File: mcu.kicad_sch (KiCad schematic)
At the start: 24 parts, among them J2 SWD_HIL, SW1 BTN1, SW2 BTN2, U8 STM32G431MBT6

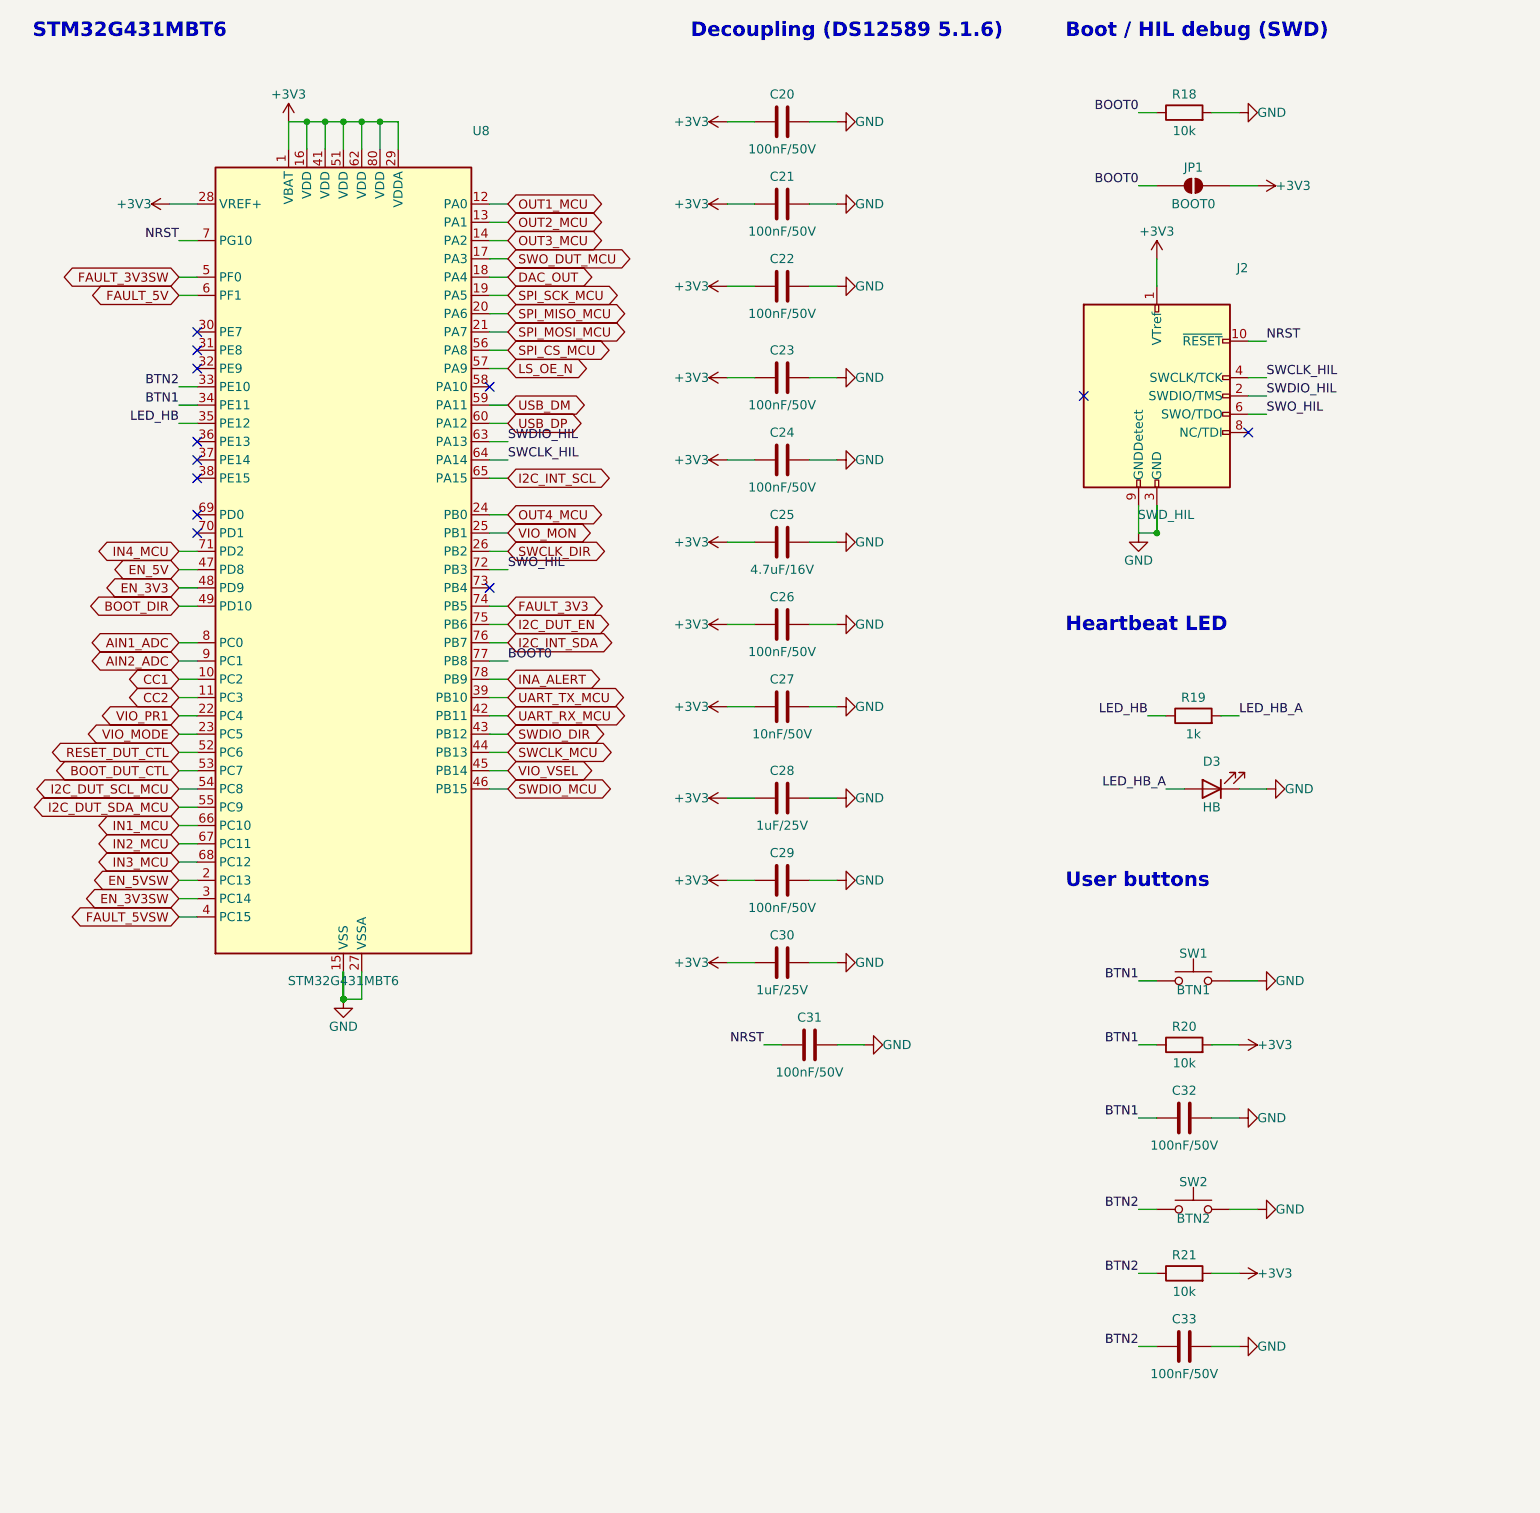
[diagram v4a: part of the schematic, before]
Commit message: feat: dual-range current sensing and fixed-rail readback in the schematic (TASK-011)
New sheets range_5v_sw, range_3v3_sw and readback appended at the end of the
hierarchy (existing references unchanged). Shunts now end on *_MID, INA226
Vin- on *_MID, MCU pins remapped per NOTES.md. ERC 0 errors, netlist and BOM
0 mismatches.

Co-Authored-By: Claude Opus 5.5 <noreply@anthropic.com>
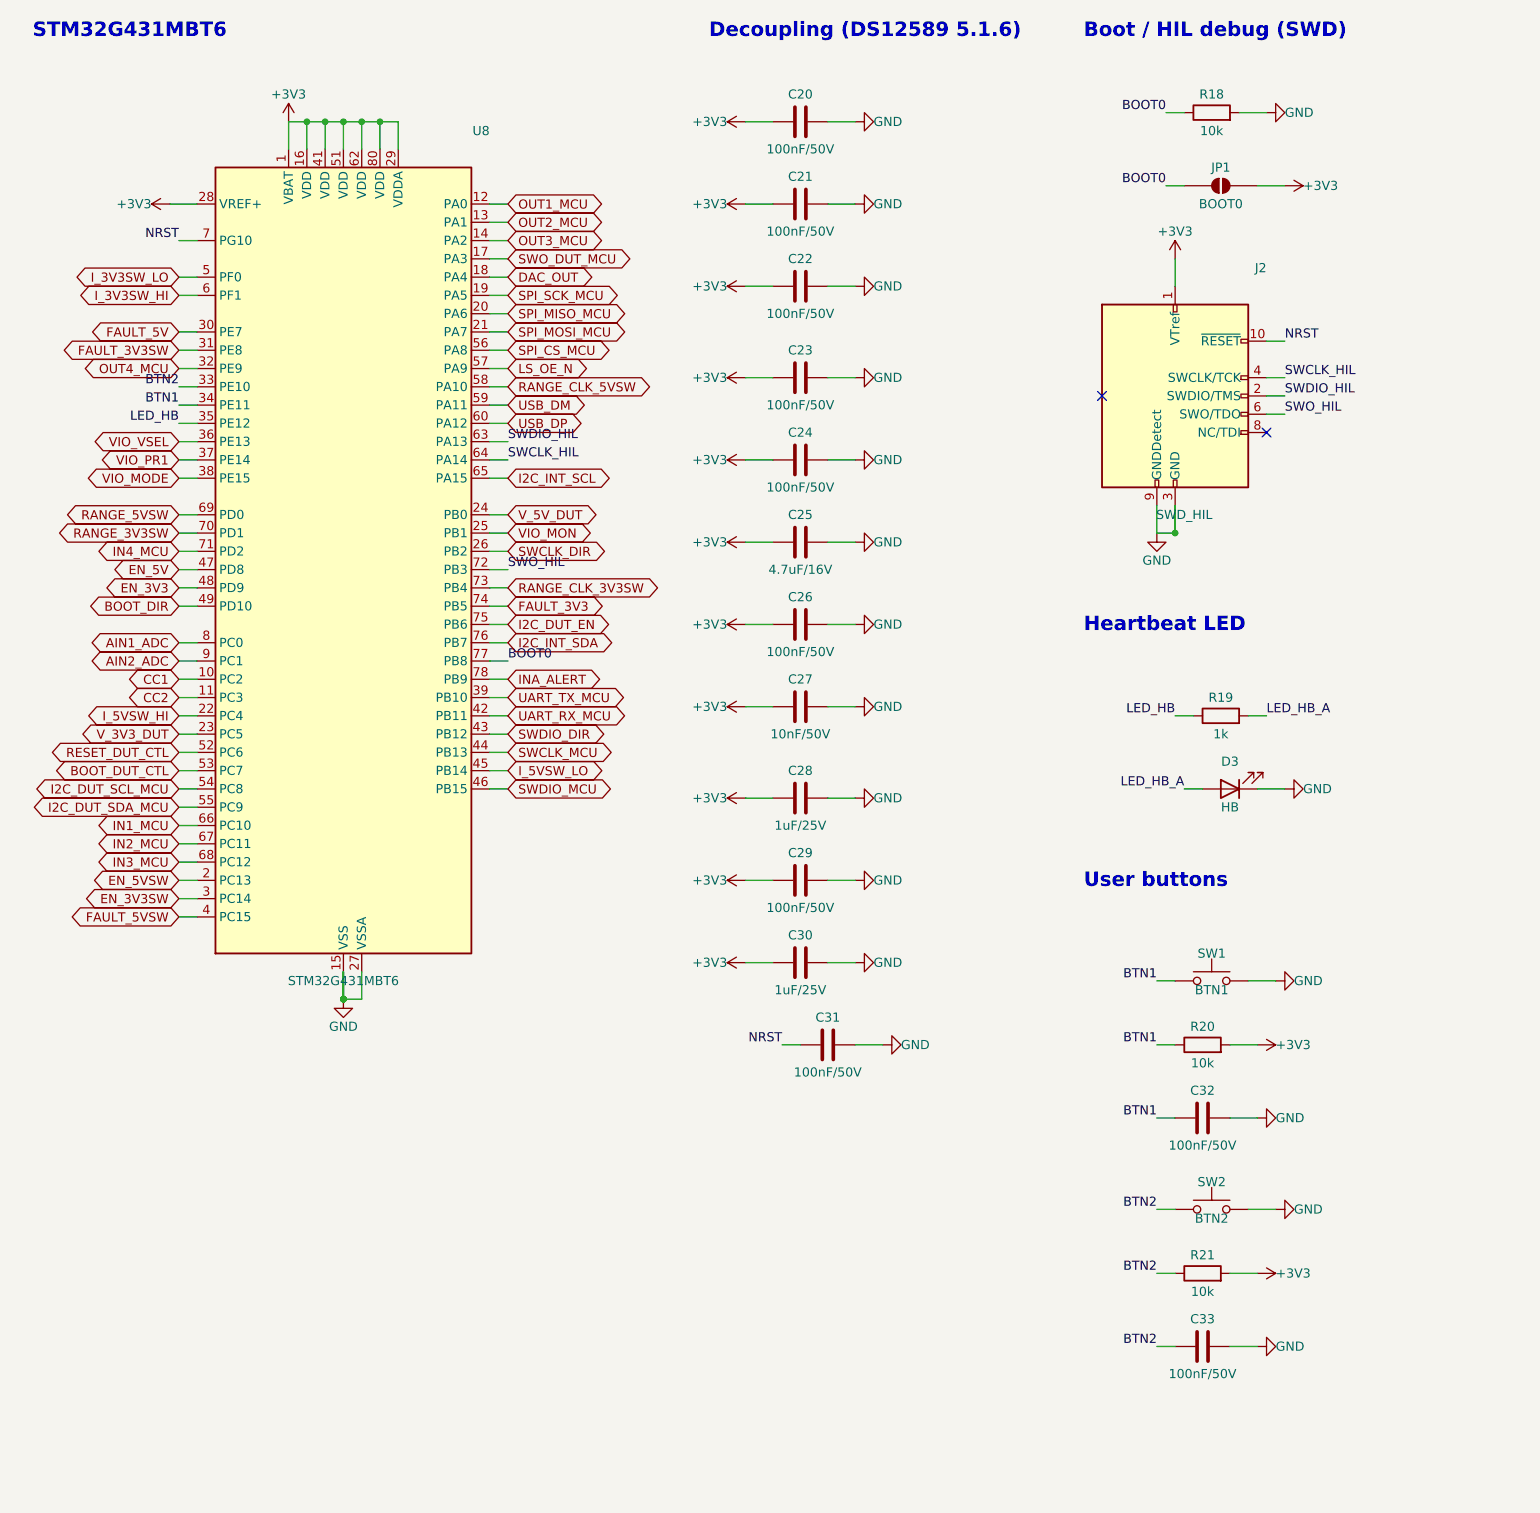
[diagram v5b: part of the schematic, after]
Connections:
- net FAULT_3V3SW: now also U8.31 (PE8); no longer U8.5 (PF0)
- net FAULT_5V: now also U8.30 (PE7); no longer U8.6 (PF1)
- net OUT4_MCU: now also U8.32 (PE9); no longer U8.24 (PB0)
- net VIO_MODE: now also U8.38 (PE15); no longer U8.23 (PC5)
- net VIO_PR1: now also U8.37 (PE14); no longer U8.22 (PC4)
- net VIO_VSEL: now also U8.36 (PE13); no longer U8.45 (PB14)
- net RANGE_CLK_5VSW: now reaches U8.58 (PA10)
- net RANGE_5VSW: now reaches U8.69 (PD0)
- net RANGE_3V3SW: now reaches U8.70 (PD1)
- net RANGE_CLK_3V3SW: now reaches U8.73 (PB4)
- new net I_3V3SW_HI: U8.6 (PF1)
- new net I_3V3SW_LO: U8.5 (PF0)
- new net I_5VSW_HI: U8.22 (PC4)
- new net I_5VSW_LO: U8.45 (PB14)
- new net V_3V3_DUT: U8.23 (PC5)
- new net V_5V_DUT: U8.24 (PB0)
- no-connect marks 12 -> 2
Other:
- moved on the sheet: C20, C21, C22, C23, C24, C25, C26, C27, C28, C29, C30, C31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

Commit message: fix: schematic review of TASK-011 (DNP cap part number, parallel-path note, UCPD/PB4 note)
Co-Authored-By: Claude Opus 5.5 <noreply@anthropic.com>
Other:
- note added: "PB6 may carry a UCPD dead-battery pull-down at reset (PA9 = DBCC1 is pulled high); I2C_DUT_EN has an external pull-down anyway. Same for PB4 (CC2): PA10 = DBCC2 is held low by the 100k on RANGE_CLK_5VSW; PB4 also has the NJTRST pull-up at reset. Firmware sets PWR_CR3.UCPD1_DBDIS first, then drives PB4 low."
- note removed: "PB6 may carry a UCPD dead-battery pull-down at reset (PA9 = DBCC1 is pulled high); I2C_DUT_EN has an external pull-down anyway. Firmware sets PWR_CR3.UCPD1_DBDIS first."
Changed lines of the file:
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@@
 		)
 	)
-	(text "PB6 may carry a UCPD dead-battery pull-down at reset (PA9 = DBCC1 is pulled high); I2C_DUT_EN has an external pull-down anyway. Firmware sets PWR_CR3.UCPD1_DBDIS first."
+	(text "PB6 may carry a UCPD dead-battery pull-down at reset (PA9 = DBCC1 is pulled high); I2C_DUT_EN has an external pull-down anyway. Same for PB4 (CC2): PA10 = DBCC2 is held low by the 100k on RANGE_CLK_5VSW; PB4 also has the NJTRST pull-up at reset. Firmware sets PWR_CR3.UCPD1_DBDIS first, then drives PB4 low."
 		(exclude_from_sim no)
 		(at 20 260.35 0)
